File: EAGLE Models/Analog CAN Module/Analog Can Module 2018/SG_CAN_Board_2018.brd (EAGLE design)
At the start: 160 x 100 mm, 104 parts, among them IC1 AT90CAN128, IC2 MCP2551SO8, IC3 NUP2105L, IC5 FT232RL, Q1 56P2859, U1 LTC2053, U11 LTC2053, U12 LTC2053, U2 LTC2053, U3 LTC2053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

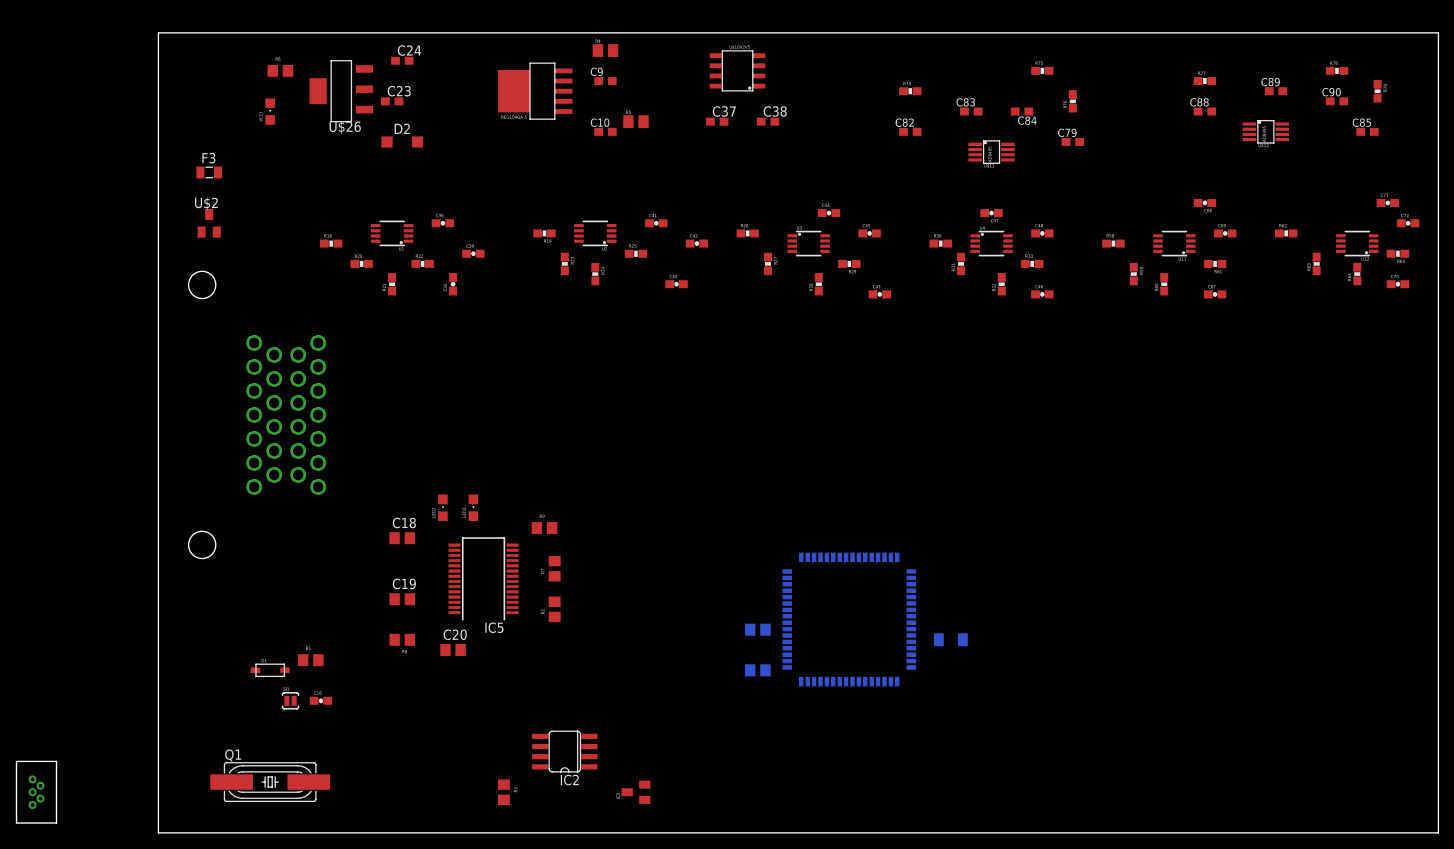
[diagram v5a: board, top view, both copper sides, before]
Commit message: SG CAN Board
90% done routing.
Will continue tomorrow.
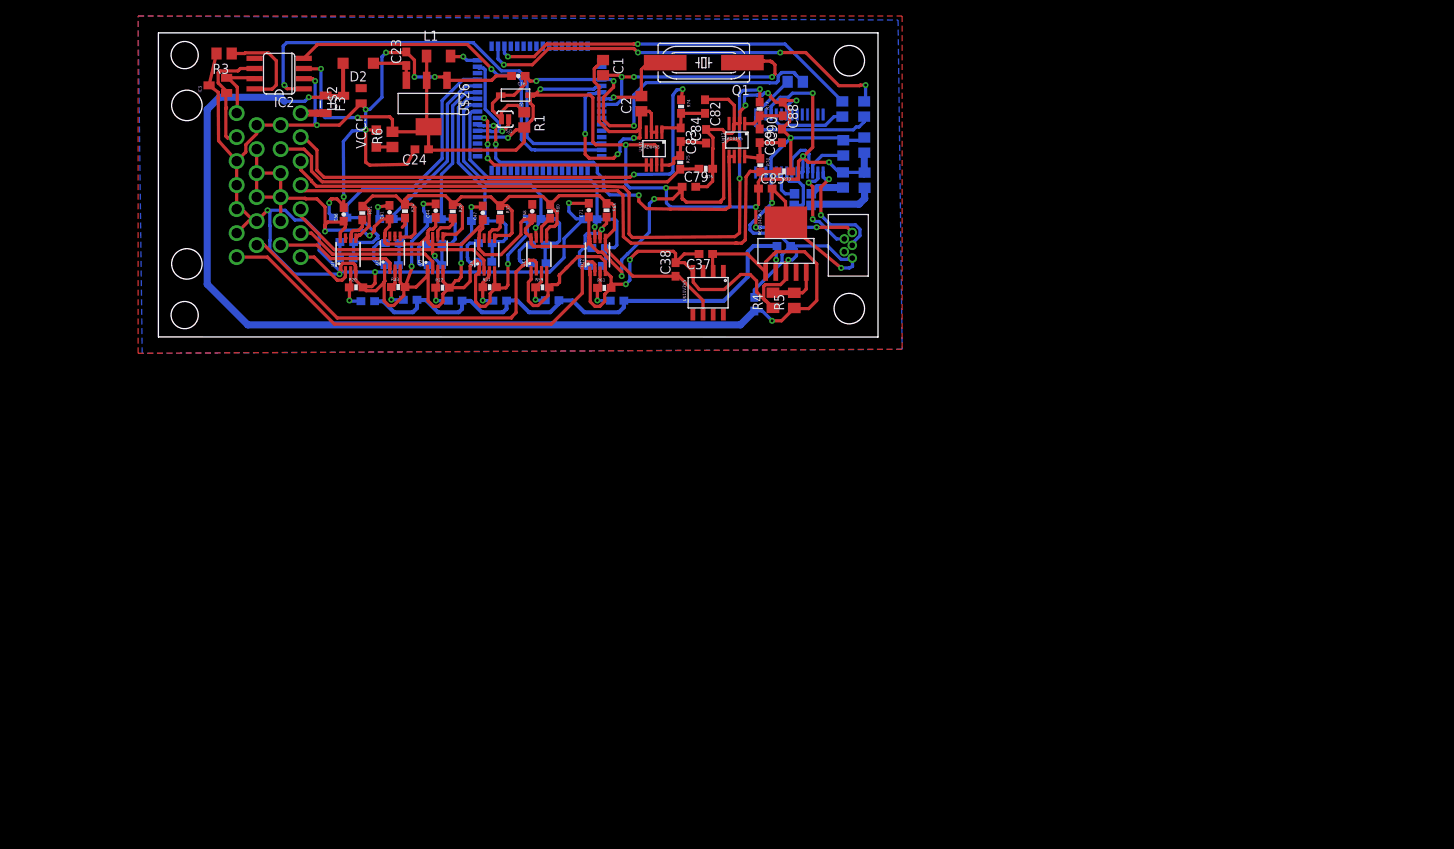
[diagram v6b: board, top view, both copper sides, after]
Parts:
- C10, C79, C82, C83, C84, C85, C88, C89, C9, C90: device rcl:C0603@1 -> rcl:C0603
- moved U$4 122.4 mm to (86.2, 73.4), turned to 180 degrees
- moved Q1 105.0 mm to (68.2, 96.3), turned to 180 degrees
- moved IC3 102.7 mm to (7.43, 93.4)
- moved C72 102.2 mm to (54.0, 76.7), flipped to the bottom, turned to 180 degrees
- moved R65 100.3 mm to (54.6, 70.9), flipped to the bottom
- moved C70 100.0 mm to (55.0, 73.1), flipped to the bottom
- moved C71 99.9 mm to (53.8, 77.8), turned to 90 degrees
- moved R3 98.7 mm to (8.21, 97.4), turned to 180 degrees
- moved L1 97.1 mm to (35.0, 97.1), flipped to the top
- moved U12 95.0 mm to (54.9, 72.3), turned to 0 degrees
- moved R64 94.2 mm to (56.0, 77.8), turned to 270 degrees
- moved IC2 92.0 mm to (15.1, 94.9)
- moved R63 89.1 mm to (55.7, 68.1), turned to 0 degrees
- moved C69 86.4 mm to (47.0, 76.7), flipped to the bottom, turned to 180 degrees
- moved C67 84.8 mm to (47.5, 73.5), flipped to the bottom
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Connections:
- removed net 10V: C37.1, U$10V2V5.P2
- removed net 12V_PREPTC: F3.2, U$2.3
- new net N$13: F3.2, U$3.B1
- net 12V: now also C37.1, U$10V2V5.P2, U$2.3
- net GND: now also U$3.B14, U$3.B18, U$3.B8; no longer U$3.B26
- net PA0: no longer U$3.B18
- net PA1: no longer U$3.B19
- net SG_1: now also U$3.B7
- net SG_2: now also U$3.B13
- net SG_3: now also U$3.B6
- net SG_4: now also U$3.B5
- net SG_5: now also U$3.B19
- net SG_6: now also U$3.B26
- net TCI1+: now also U$3.B2; no longer U$3.B14
- net TCI1-: now also U$3.B9; no longer U$3.B15
- net TCI2+: now also U$3.B3; no longer U$3.B16
- net TCI2-: now also U$3.B4; no longer U$3.B17
- net VCC: now also U$3.B10, U$3.B11, U$3.B12, U$3.B15, U$3.B16, U$3.B17
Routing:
- net GND: track 0.00 -> 533.3 mm, vias 0 -> 32
- net VCC: track 0.00 -> 307.2 mm, vias 0 -> 16
- net 12V: track 0.00 -> 147.9 mm, vias 0 -> 2
- net 2V5REF: track 0.00 -> 90.3 mm
- net TCI2+: track 0.00 -> 84.7 mm, vias 0 -> 2
- net TCI2-: track 0.00 -> 74.1 mm
- net SG5V: track 0.00 -> 67.0 mm, vias 0 -> 1
- net TCI1+: track 0.00 -> 62.8 mm, vias 0 -> 2
- net RESET: track 0.00 -> 61.3 mm, vias 0 -> 3
- net TXCAN: track 0.00 -> 57.9 mm, vias 0 -> 1
- net TCI1-: track 0.00 -> 55.7 mm
- net SG_6: track 0.00 -> 54.4 mm
- net RX: track 0.00 -> 52.7 mm, vias 0 -> 4
- net RXCAN: track 0.00 -> 48.0 mm, vias 0 -> 1
- net TX: track 0.00 -> 46.9 mm, vias 0 -> 2
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- added copper zone on layer 1, net GND
- added copper zone on layer 16, net GND
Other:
- board size 160 x 100 mm -> 89.9 x 38 mm

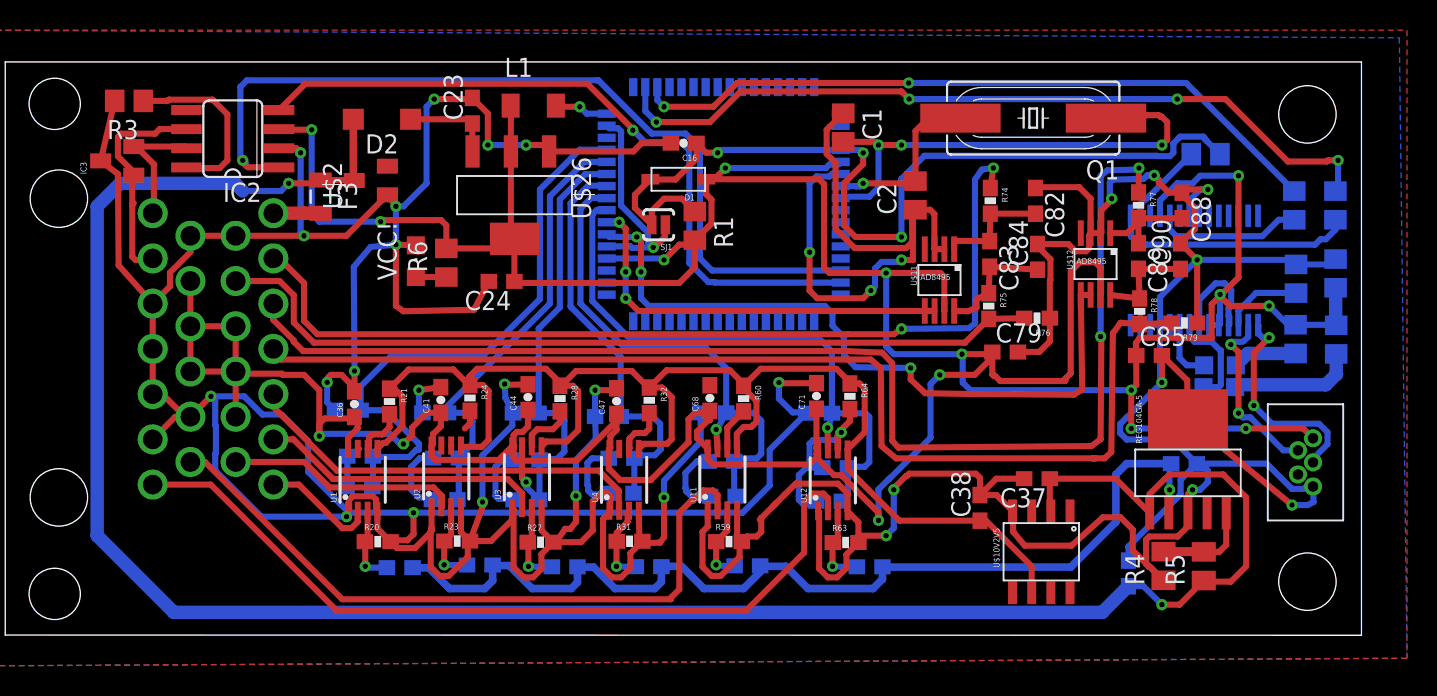
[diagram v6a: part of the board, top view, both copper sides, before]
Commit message: finished making all the connections on the SG CAN Board
few spacing and clearance issues that need to be fixed
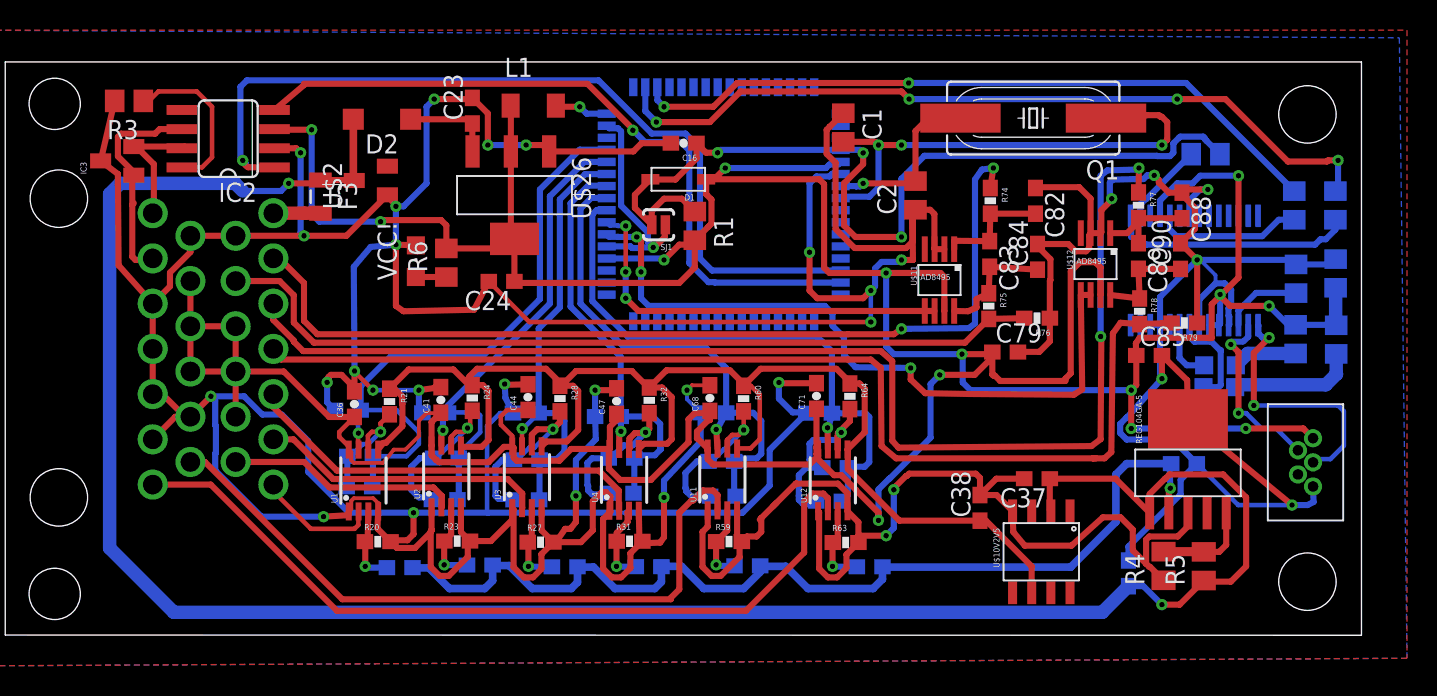
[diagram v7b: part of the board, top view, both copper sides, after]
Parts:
- moved IC2 0.30 mm to (14.8, 94.9)
- moved R24 0.15 mm to (31.0, 77.7)
- moved U1 0.07 mm to (23.8, 72.2)
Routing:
- net GND: track 533.3 -> 563.1 mm, vias 32 -> 33
- net N$7: track 6.18 -> 11.2 mm, vias 0 -> 1
- net N$29: track 7.83 -> 11.3 mm, vias 0 -> 1
- net N$10: track 8.35 -> 11.8 mm, vias 0 -> 1
- net SGO2: track 29.4 -> 32.7 mm, vias 0 -> 1
- net N$14: track 8.15 -> 11.3 mm, vias 0 -> 1
- net D+: track 14.3 -> 17.5 mm
- net N$1: track 5.93 -> 8.80 mm, vias 0 -> 1
- net SGO1: track 39.5 -> 42.4 mm, vias 0 -> 1
- net VCC: track 307.2 -> 304.4 mm, vias 16 -> 14
- net SGO4: track 27.3 -> 29.5 mm, vias 0 -> 1
- net SGO3: track 31.1 -> 29.8 mm
- net N$6: track 12.0 -> 10.9 mm
- net TCO1: track 26.1 -> 27.0 mm
- net M8TXD: track 8.91 -> 9.82 mm
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
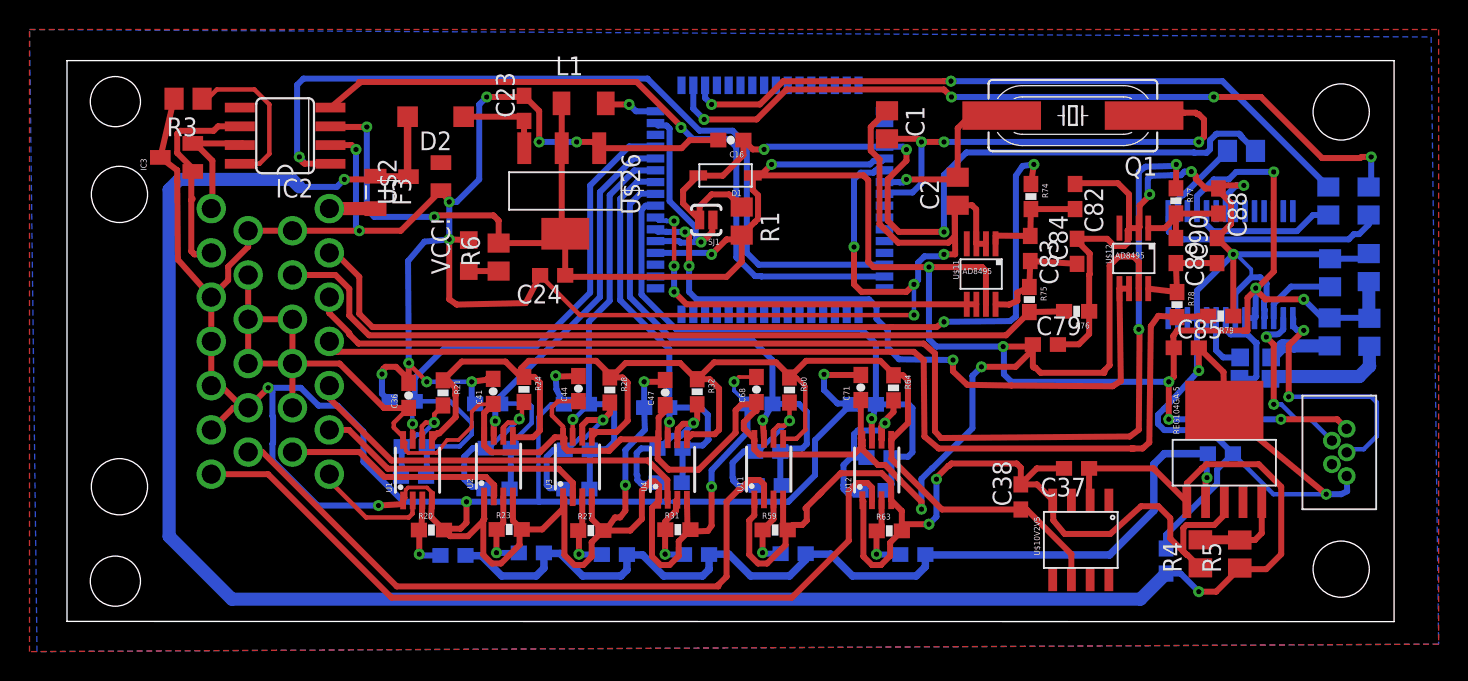
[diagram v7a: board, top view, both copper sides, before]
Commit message: Finished Board Layout For CAN Boards
USB-mini part update issues remain
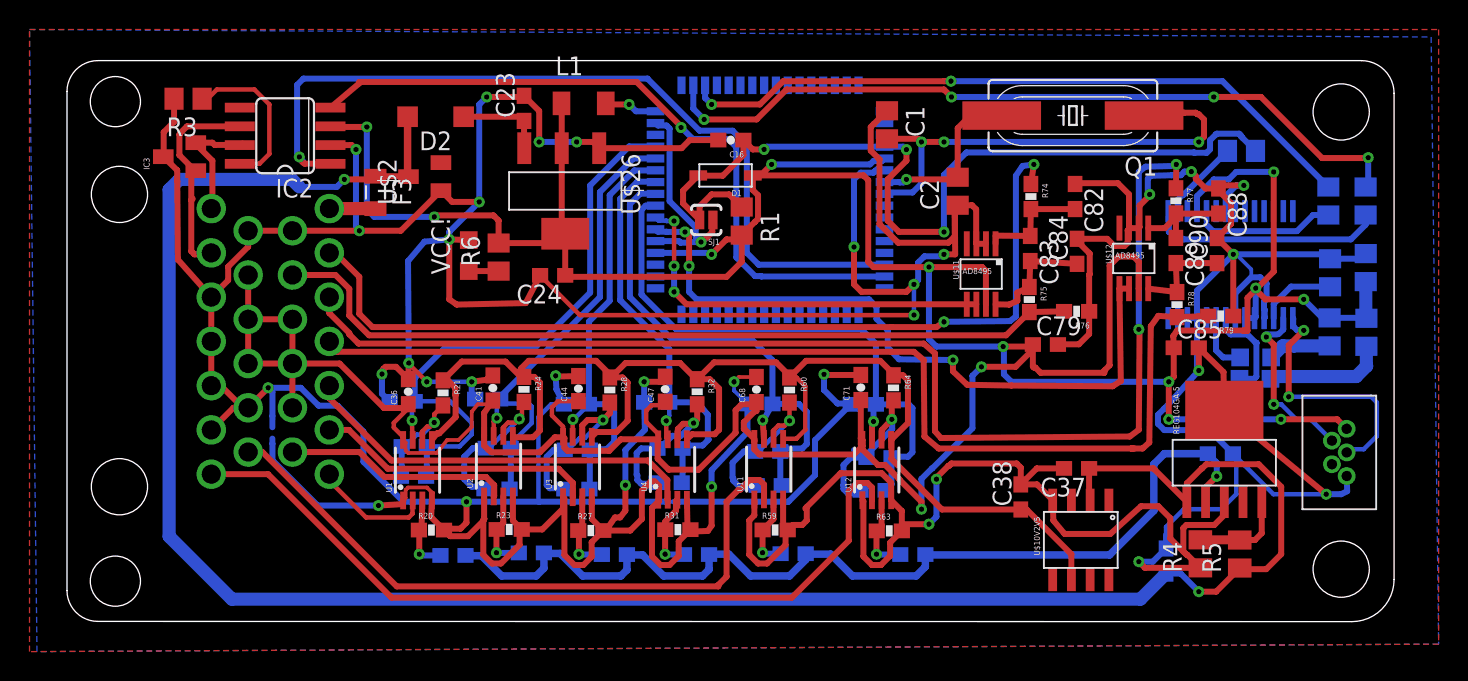
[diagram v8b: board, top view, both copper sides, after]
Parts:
- moved C48 0.36 mm to (40.0, 76.8)
- moved C42 0.33 mm to (28.5, 77.1)
- moved C36 0.26 mm to (23.1, 77.6)
- moved C41 0.23 mm to (28.9, 77.8)
- moved C47 0.23 mm to (40.5, 77.7)
- moved IC3 0.21 mm to (7.63, 93.5)
- moved C19 0.20 mm to (88.0, 86.0)
- moved R2 0.20 mm to (88.0, 90.5)
- moved R9 0.20 mm to (88.1, 81.6)
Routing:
- net GND: track 563.1 -> 571.3 mm, vias 33 -> 34
- net VCC: track 304.4 -> 306.4 mm
- net N$31: track 13.3 -> 11.9 mm
- net SGO4: track 29.5 -> 30.1 mm
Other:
- outline, holes or cut-outs redrawn
